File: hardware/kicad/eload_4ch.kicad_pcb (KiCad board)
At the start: 2 copper layers, 170 x 125 mm, 142 parts, among them J1 DUT+, J2 DUT-, J3 SENSE, J4 D1mini L, J5 D1mini R, J6 FRONT PANEL, J7 FAN, J8 NTC, J9 12V DC, Q1 IXTH75N10L2, Q2 IXTH75N10L2, Q3 IXTH75N10L2, Q4 IXTH75N10L2, Q5 FDS9926A, Q6 FDS9926A, Q7 FDS9926A, U1 TL431ID, U10 DAC8565, U11 L78L05, U12 AP63205WU, U2 LM393, U3 OPA2196, U4 INA228, U5 INA228, U6 OPA2196, U7 INA228, U8 INA228, U9 PCF8574T

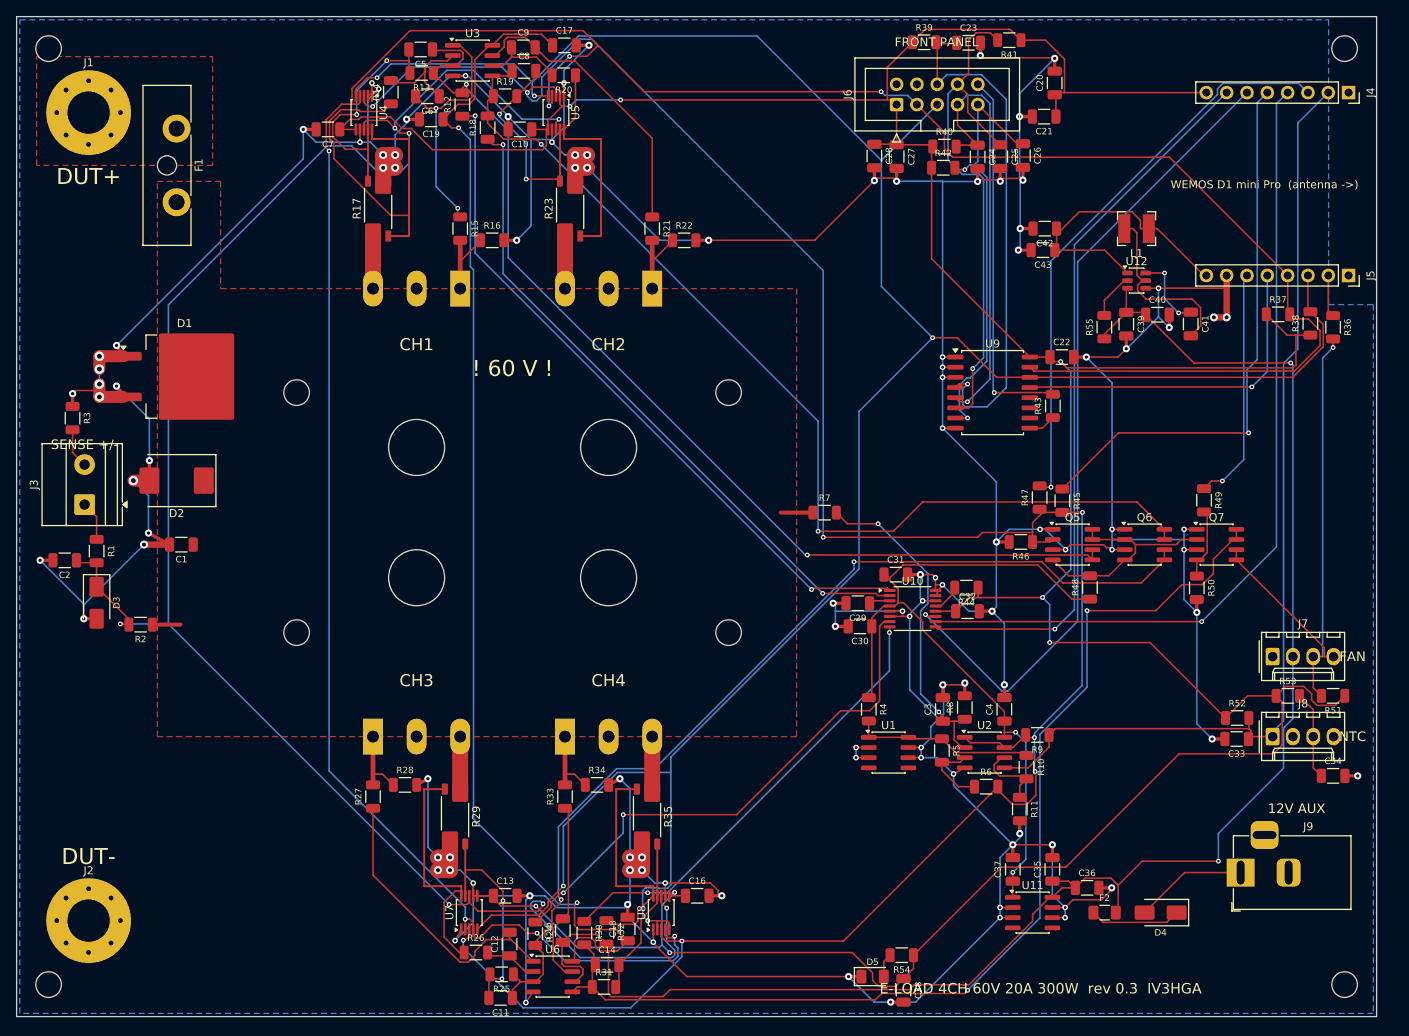
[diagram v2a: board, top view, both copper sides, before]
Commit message: Clean silkscreen and add assembly aids
Reference designators repositioned next to their parts with no overlap
on pads, other silkscreen or component bodies (relabel.py); dangling
track stubs cleaned (cleanup.py). DRC: only the 4 intentional MOSFET
footprint overrides remain. Added interactive HTML BOM and top/bottom
assembly drawings.

Co-Authored-By: Claude Opus 5.5 <noreply@anthropic.com>
Claude-Session: https://claude.ai/code/session_013KrwoEq2Y4F9LNKutY5RJ4
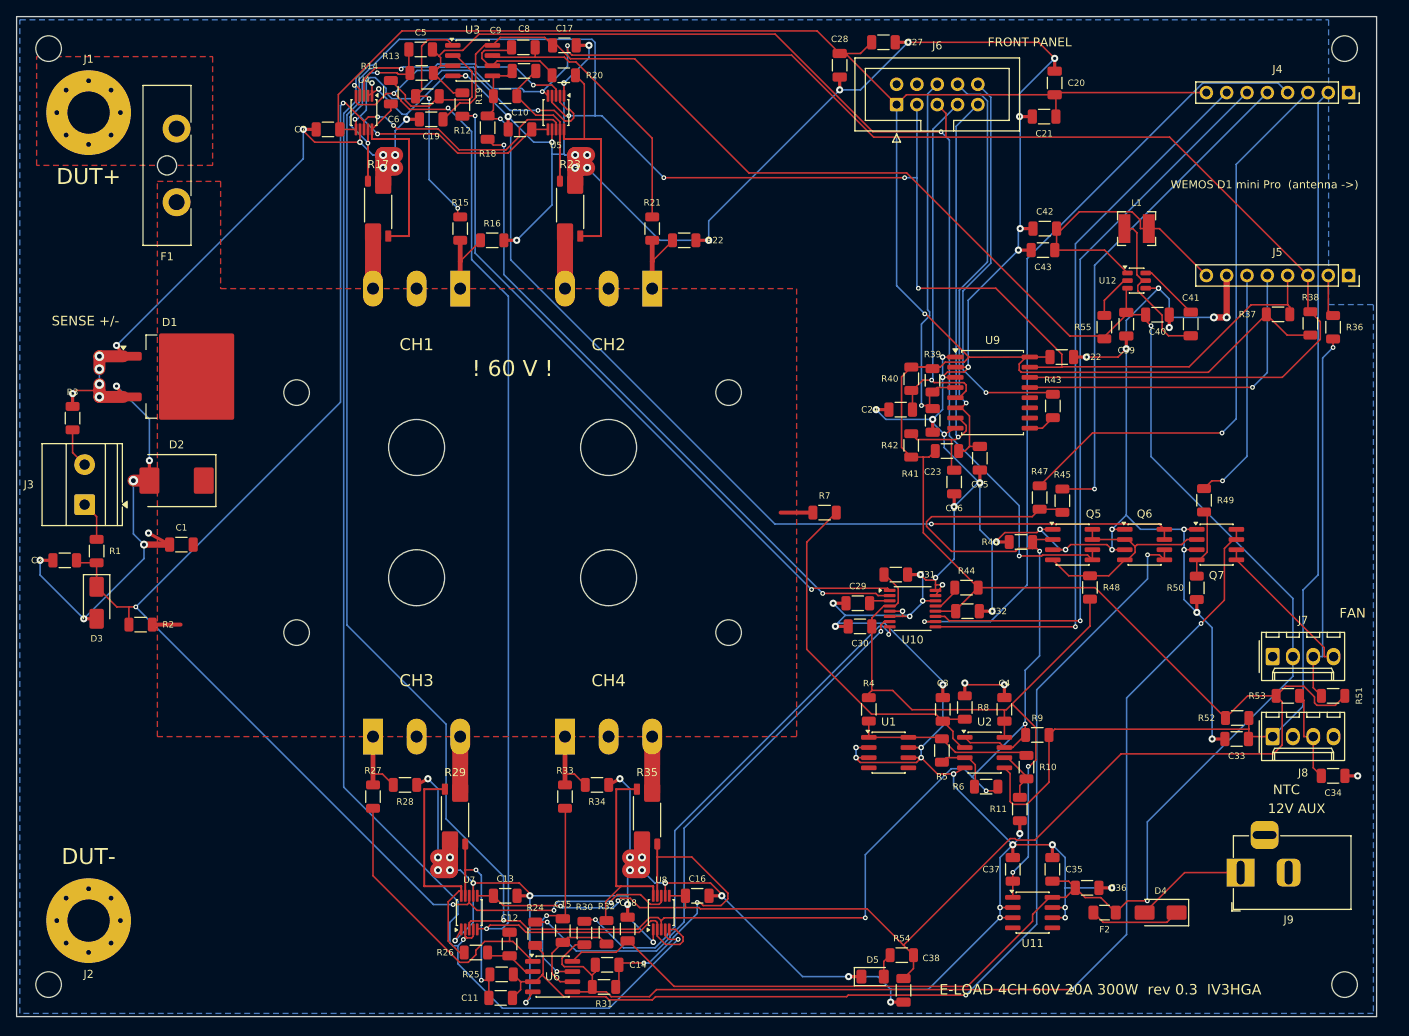
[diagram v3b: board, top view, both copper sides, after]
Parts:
- moved R41 51.9 mm to (166.3, 94.3), turned to 0 degrees
- moved C23 47.4 mm to (164.5, 90.5), turned to -90 degrees
- moved R39 42.3 mm to (164.5, 85.5), turned to -90 degrees
- moved C26 41.7 mm to (167.2, 98.2)
- moved C25 37.8 mm to (170.4, 95.2)
- moved R42 34.9 mm to (161.8, 93.6), turned to 90 degrees
- moved C24 33.0 mm to (160.5, 89.1), turned to 180 degrees
- moved R40 29.3 mm to (161.8, 85.3), turned to -90 degrees
- moved C27 14.4 mm to (158.4, 43.2), turned to 0 degrees
- moved C28 12.1 mm to (152.9, 46.1)
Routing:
- net +3V3: track 459.4 -> 523.9 mm, vias 8 -> 6
- net +12V: track 343.7 -> 290.0 mm, vias 4 -> 2
- net I2C_SCL: track 309.5 -> 339.6 mm
- net VSENSE: track 232.7 -> 206.5 mm
- net /Power channels/SHP1: track 46.5 -> 24.7 mm
- net /Power channels/SHN4: track 20.0 -> 39.1 mm, vias 0 -> 2
- net VSET1: track 128.9 -> 146.7 mm
- net /Control/FP_ENC_A: track 65.3 -> 47.7 mm
- net GND: track 858.1 -> 875.6 mm
- net /Control/FP_ENC_SW: track 66.7 -> 53.9 mm
- net VSET3: track 120.8 -> 133.5 mm
- net ARM: track 299.1 -> 311.5 mm, vias 8 -> 7
- net /Control/SPI_MOSI: track 102.8 -> 93.0 mm
- net I2C_SDA: track 348.4 -> 338.7 mm
- net /Power channels/SHN2: track 27.5 -> 18.3 mm, vias 2 -> 0
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
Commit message: Add IV3HGA logo to schematic sheets and PCB silkscreen
Logo next to the title block on every sheet; 25 mm silkscreen version
(board-only footprint eload:Logo_IV3HGA_25mm in the project library).
ERC/DRC unchanged: no silkscreen overlaps, schematic parity clean.

Co-Authored-By: Claude Opus 5.5 <noreply@anthropic.com>
Claude-Session: https://claude.ai/code/session_013KrwoEq2Y4F9LNKutY5RJ4
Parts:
- added LOGO1: Logo_IV3HGA, eload:Logo_IV3HGA_25mm, F.Cu at (159.9, 69.4)
